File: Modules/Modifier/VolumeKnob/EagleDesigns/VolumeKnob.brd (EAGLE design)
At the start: 100 x 80 mm, 7 parts, among them U1 TINY85-20-DIP

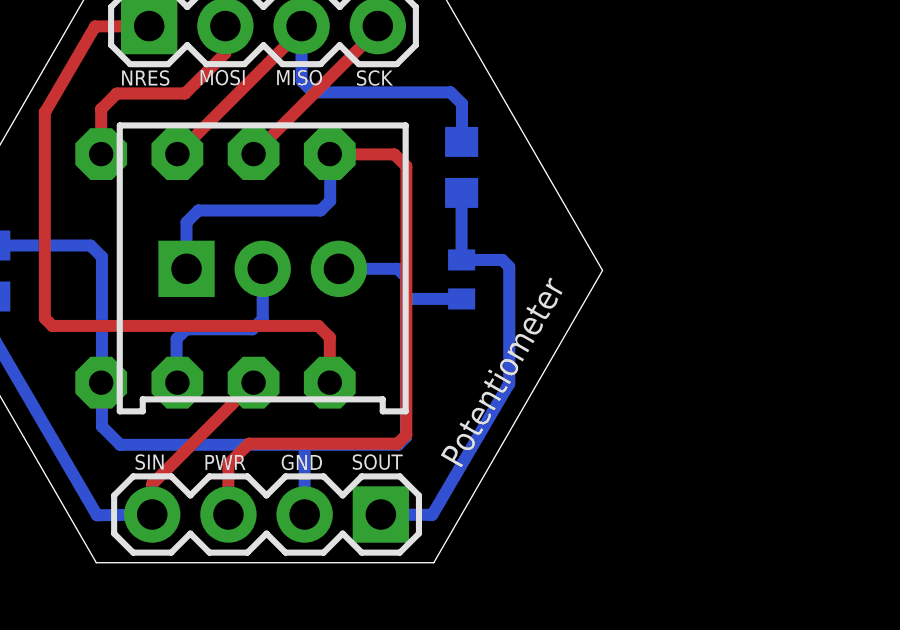
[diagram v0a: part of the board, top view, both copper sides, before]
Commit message: changed 0403 cap to 0603 SMD cap
to solder without difficulty!
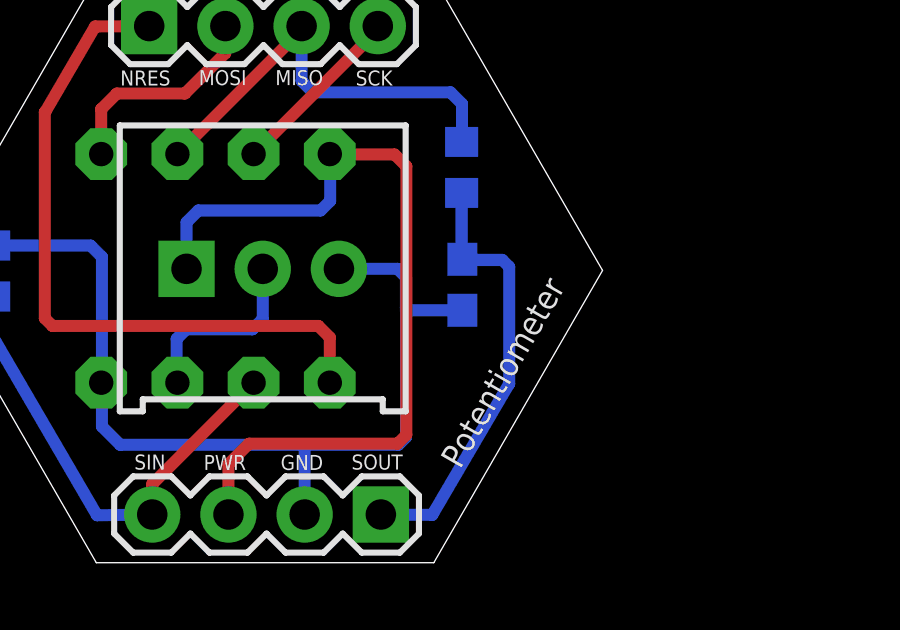
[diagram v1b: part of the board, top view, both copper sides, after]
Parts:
- removed C1: 0.22uF, adafruit:C0402
- added C2: 0.22uF, adafruit:C0603
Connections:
- net 1X3SOUT: now also C2.1; no longer C1.2
- net GND: now also C2.2; no longer C1.1
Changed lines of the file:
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@@
 <attribute name="VALUE" x="21.4249" y="17.3863" size="0.6" layer="28" rot="MR0"/>
 </element>
-<element name="C1" library="adafruit" package="C0402" value="0.22uF" x="20.6248" y="11.938" smashed="yes" rot="MR90">
-<attribute name="VALUE" x="21.4249" y="10.8204" size="0.6" layer="28" rot="MR90"/>
-</element>
+<element name="C2" library="adafruit" package="C0603" value="0.22uF" x="20.6502" y="11.7602" rot="MR270"/>
 </elements>
 <signals>
@@
 <contactref element="POT1" pad="3"/>
 <contactref element="R1" pad="1"/>
-<contactref element="C1" pad="1"/>
 <wire x1="16.5354" y1="12.2913" x2="18.4935" y2="12.2913" width="0.4" layer="16"/>
-<wire x1="18.4935" y1="12.2913" x2="18.7706" y2="12.0142" width="0.4" layer="16"/>
-<wire x1="18.7706" y1="12.0142" x2="18.7706" y2="11.2014" width="0.4" layer="16"/>
-<wire x1="18.7706" y1="11.2014" x2="18.7706" y2="6.6802" width="0.4" layer="16"/>
+<wire x1="18.7706" y1="10.8712" x2="18.7706" y2="6.6802" width="0.4" layer="16"/>
 <wire x1="18.7706" y1="6.6802" x2="18.5166" y2="6.4262" width="0.4" layer="16"/>
-<wire x1="20.6248" y1="11.288" x2="18.8572" y2="11.288" width="0.4" layer="16"/>
-<wire x1="18.8572" y1="11.288" x2="18.7706" y2="11.2014" width="0.4" layer="16"/>
 <wire x1="18.5166" y1="6.4262" x2="15.2781" y2="6.4262" width="0.4" layer="16"/>
 <wire x1="15.2781" y1="6.4262" x2="9.2456" y2="6.4262" width="0.4" layer="16"/>
@@
 <wire x1="8.636" y1="12.6873" x2="8.636" y2="8.5217" width="0.4" layer="16"/>
 <wire x1="8.636" y1="8.5217" x2="8.6106" y2="8.4963" width="0.4" layer="16"/>
+<contactref element="C2" pad="2"/>
+<wire x1="18.7706" y1="10.8712" x2="18.7706" y2="10.9982" width="0.4064" layer="16"/>
+<wire x1="18.7706" y1="10.9982" x2="18.7706" y2="12.0142" width="0.4064" layer="16"/>
+<wire x1="18.7706" y1="12.0142" x2="18.4935" y2="12.2913" width="0.4064" layer="16"/>
+<wire x1="20.6502" y1="10.9102" x2="18.8586" y2="10.9102" width="0.4064" layer="16"/>
+<wire x1="18.8586" y1="10.9102" x2="18.7706" y2="10.9982" width="0.4064" layer="16"/>
 </signal>
 <signal name="1X3SOUT">
 <contactref element="JP1" pad="1"/>
 <contactref element="R2" pad="1"/>
-<contactref element="C1" pad="2"/>
-<wire x1="20.6248" y1="14.8218" x2="20.6248" y2="12.588" width="0.4" layer="16"/>
-<wire x1="20.6248" y1="12.588" x2="21.9814" y2="12.588" width="0.4" layer="16"/>
 <wire x1="21.9814" y1="12.588" x2="22.2123" y2="12.3571" width="0.4" layer="16"/>
 <wire x1="22.2123" y1="12.3571" x2="22.2123" y2="8.4582" width="0.4" layer="16"/>
@@
 <wire x1="22.1996" y1="8.4455" x2="19.6469" y2="4.0894" width="0.4" layer="16"/>
 <wire x1="19.6469" y1="4.0894" x2="17.9324" y2="4.1021" width="0.4" layer="16"/>
+<contactref element="C2" pad="1"/>
+<wire x1="21.9814" y1="12.588" x2="20.6502" y2="12.588" width="0.4064" layer="16"/>
+<wire x1="20.6502" y1="12.588" x2="20.6502" y2="12.6102" width="0.4064" layer="16"/>
+<wire x1="20.6502" y1="12.6102" x2="20.6248" y2="12.6102" width="0.4064" layer="16"/>
+<wire x1="20.6248" y1="12.6102" x2="20.6248" y2="14.8218" width="0.4064" layer="16"/>
 </signal>
 <signal name="N$1">
